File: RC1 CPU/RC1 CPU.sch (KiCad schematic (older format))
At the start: 43 parts, among them J1 Expansion, J2 RC1_UI_Port, J3 BARREL_JACK, M1 Mounting, M2 Mounting, M3 Mounting, M4 Mounting, U1 WD65C02, U2 HM62256BLP-7, U3 28C256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

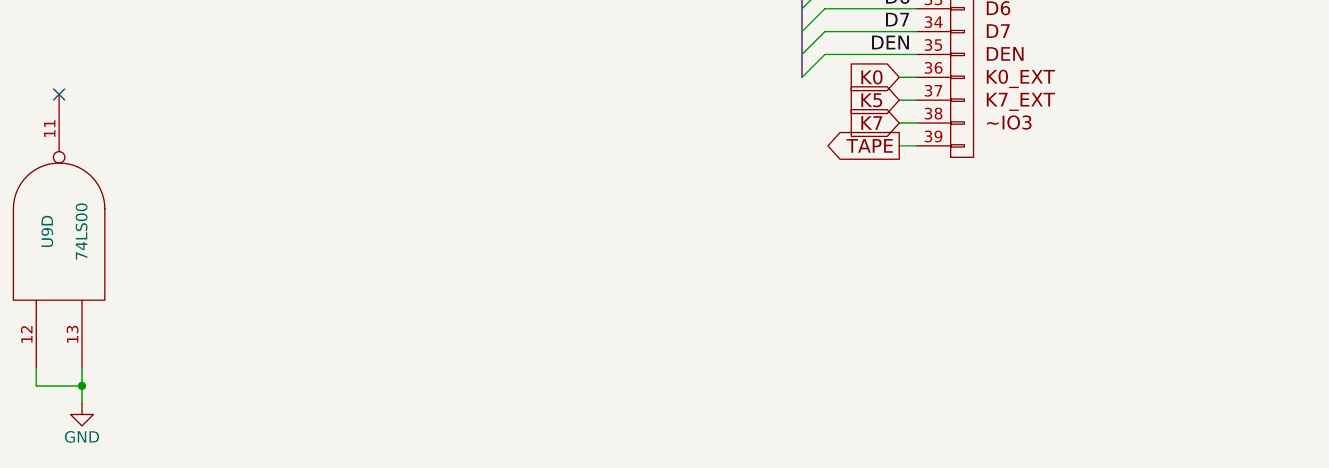
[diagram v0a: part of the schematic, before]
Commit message: Tweaked silkscreens and exported gerbers for CPU/UI
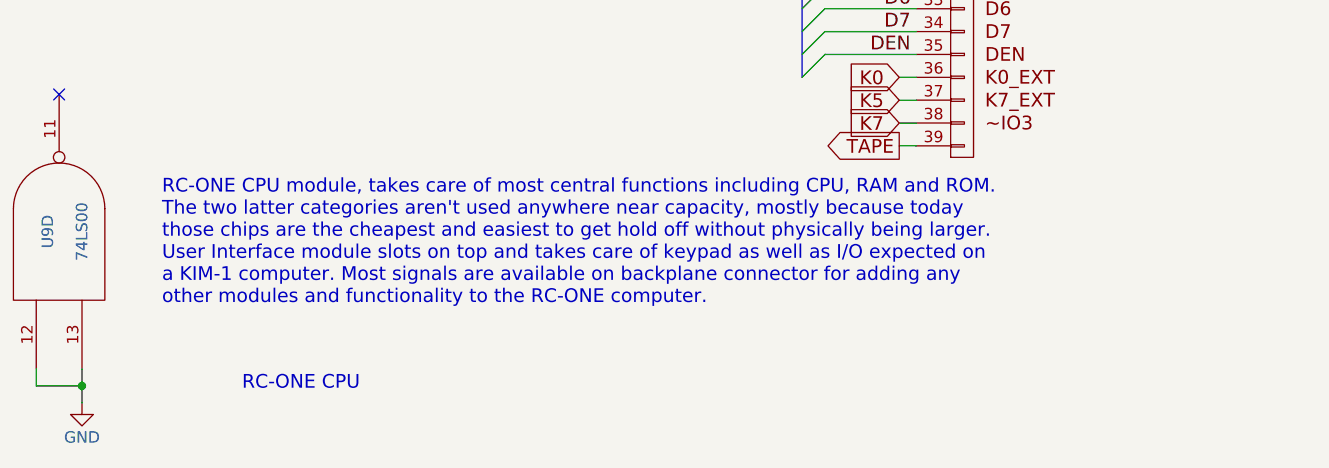
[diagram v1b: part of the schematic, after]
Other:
- note added: "RC-ONE CPU"
- note added: "RC-ONE CPU module, takes care of most central functions including CPU, RAM and ROM.\nThe two latter categories aren't used anywhere near capacity, mostly because today\nthose chips are the cheapest and easiest to get hold off without physically being larger.\nUser Interface module slots on top and takes care of keypad as well as I/O expected on\na KIM-1 computer. Most signals are available on bac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"
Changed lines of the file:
@@
 Wire Wire Line
 	5925 9375 5650 9375
+Text Notes 12175 10925 0    60   ~ 0
+RC-ONE CPU
+Text Notes 11825 10550 0    60   ~ 0
+RC-ONE CPU module, takes care of most central functions including CPU, RAM and ROM.\nThe two latter categories aren't used anywhere near capacity, mostly because today\nthose chips are the cheapest and easiest to get hold off without physically being larger.\nUser Interface module slots on top and takes care of keypad as well as I/O expected on\na KIM-1 computer. Most signals are available on backplane connector for adding any\nother modules and functionality to the RC-ONE computer.
 $EndSCHEMATC

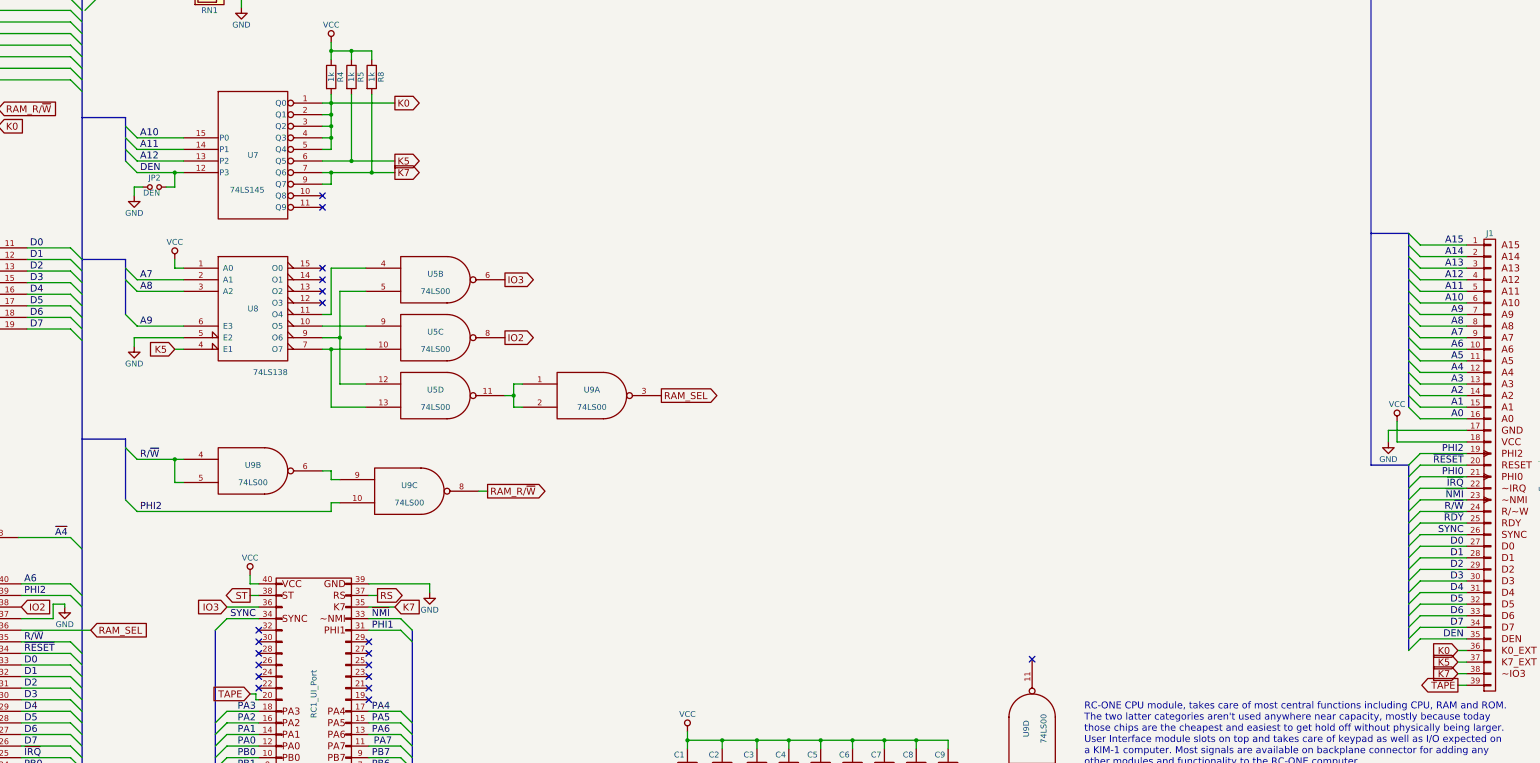
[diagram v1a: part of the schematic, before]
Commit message: Added ability to override K0/K7
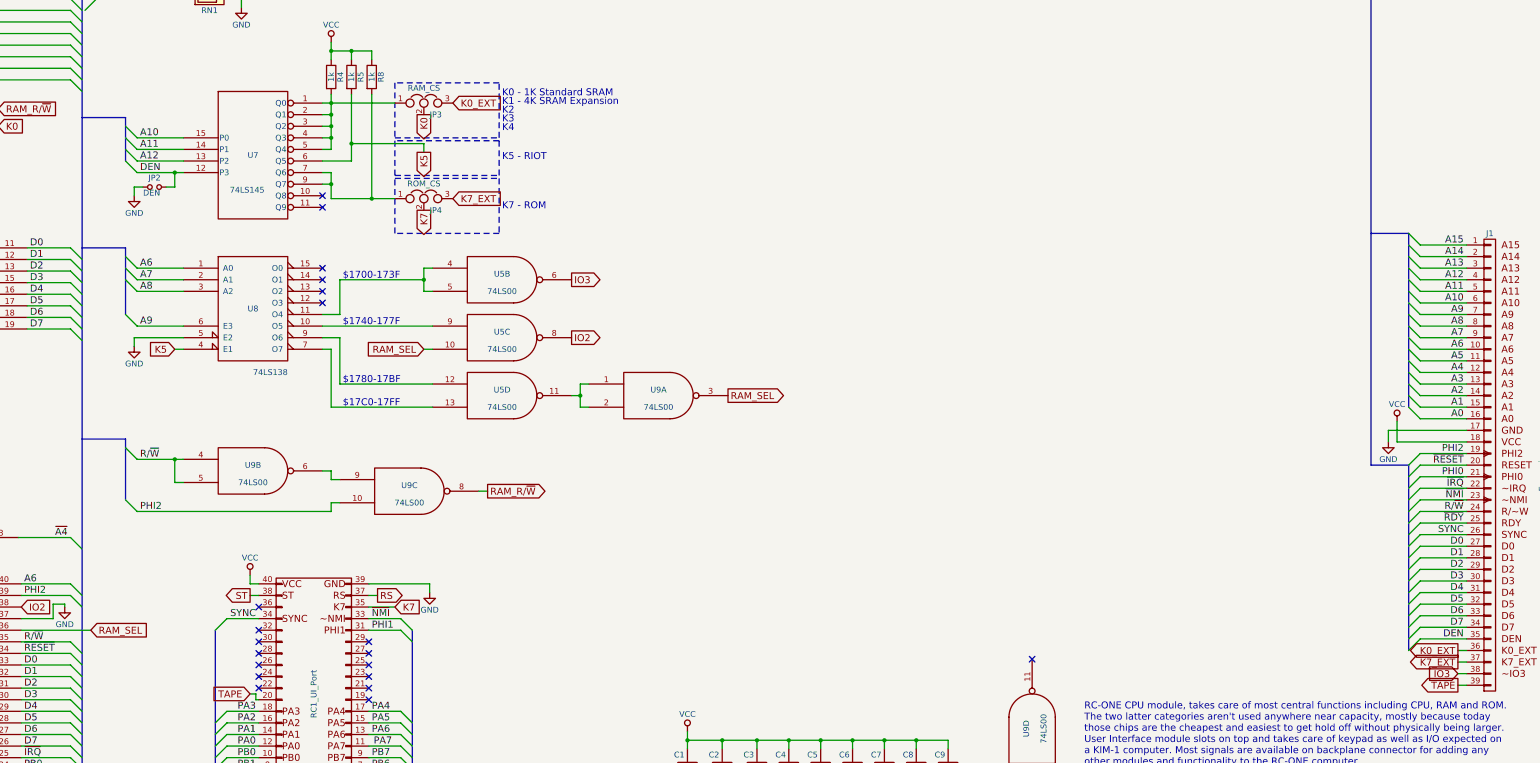
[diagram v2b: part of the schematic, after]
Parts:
- added JP3: RAM_CS, Pin_Headers:Pin_Header_Straight_1x03_Pitch2.54mm, symbol Jumper_NC_Dual
- added JP4: ROM_CS, Pin_Headers:Pin_Header_Straight_1x03_Pitch2.54mm, symbol Jumper_NC_Dual
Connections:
- net A6: now also U8.1 (A0)
- net IO3: now also J1.38 (P38); no longer J2.36 (P36)
- net K0: now also JP3.2; no longer J1.36 (RX), R4.2, U7.1 (Q0), U7.2 (Q1), U7.3 (Q2), U7.4 (Q3), U7.5 (Q4)
- net K5: no longer J1.37 (NMI)
- net K7: now also JP4.2; no longer J1.38 (P38), R8.2, U7.7 (Q6), U7.9 (Q7)
- net RAM_SEL: now also U5.10
- net VCC: no longer U8.1 (A0)
- net at U5.4, U8.11 (O4): now also U5.5
- net at U5.13, U8.7 (O7): no longer U5.10
- net at U5.12, U8.9 (O6): no longer U5.5
- new net: JP3.1, R4.2, U7.1 (Q0), U7.2 (Q1), U7.3 (Q2), U7.4 (Q3), U7.5 (Q4)
- new net: JP4.1, R8.2, U7.7 (Q6), U7.9 (Q7)
- new net K0_EXT: J1.36 (RX), JP3.3
- new net K7_EXT: J1.37 (NMI), JP4.3
- no-connect marks 25 -> 26
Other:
- note added: "$1700-173F"
- note added: "$1740-177F"
- note added: "$1780-17BF"
- note added: "$17C0-17FF"
- note added: "K0 - 1K Standard SRAM"
- note added: "K1 - 4K SRAM Expansion"
- note added: "K2"
- note added: "K3"
- note added: "K4"
- note added: "K5 - RIOT"
- note added: "K7 - ROM"
- moved on the sheet: U5B, U5C, U5D, U9A

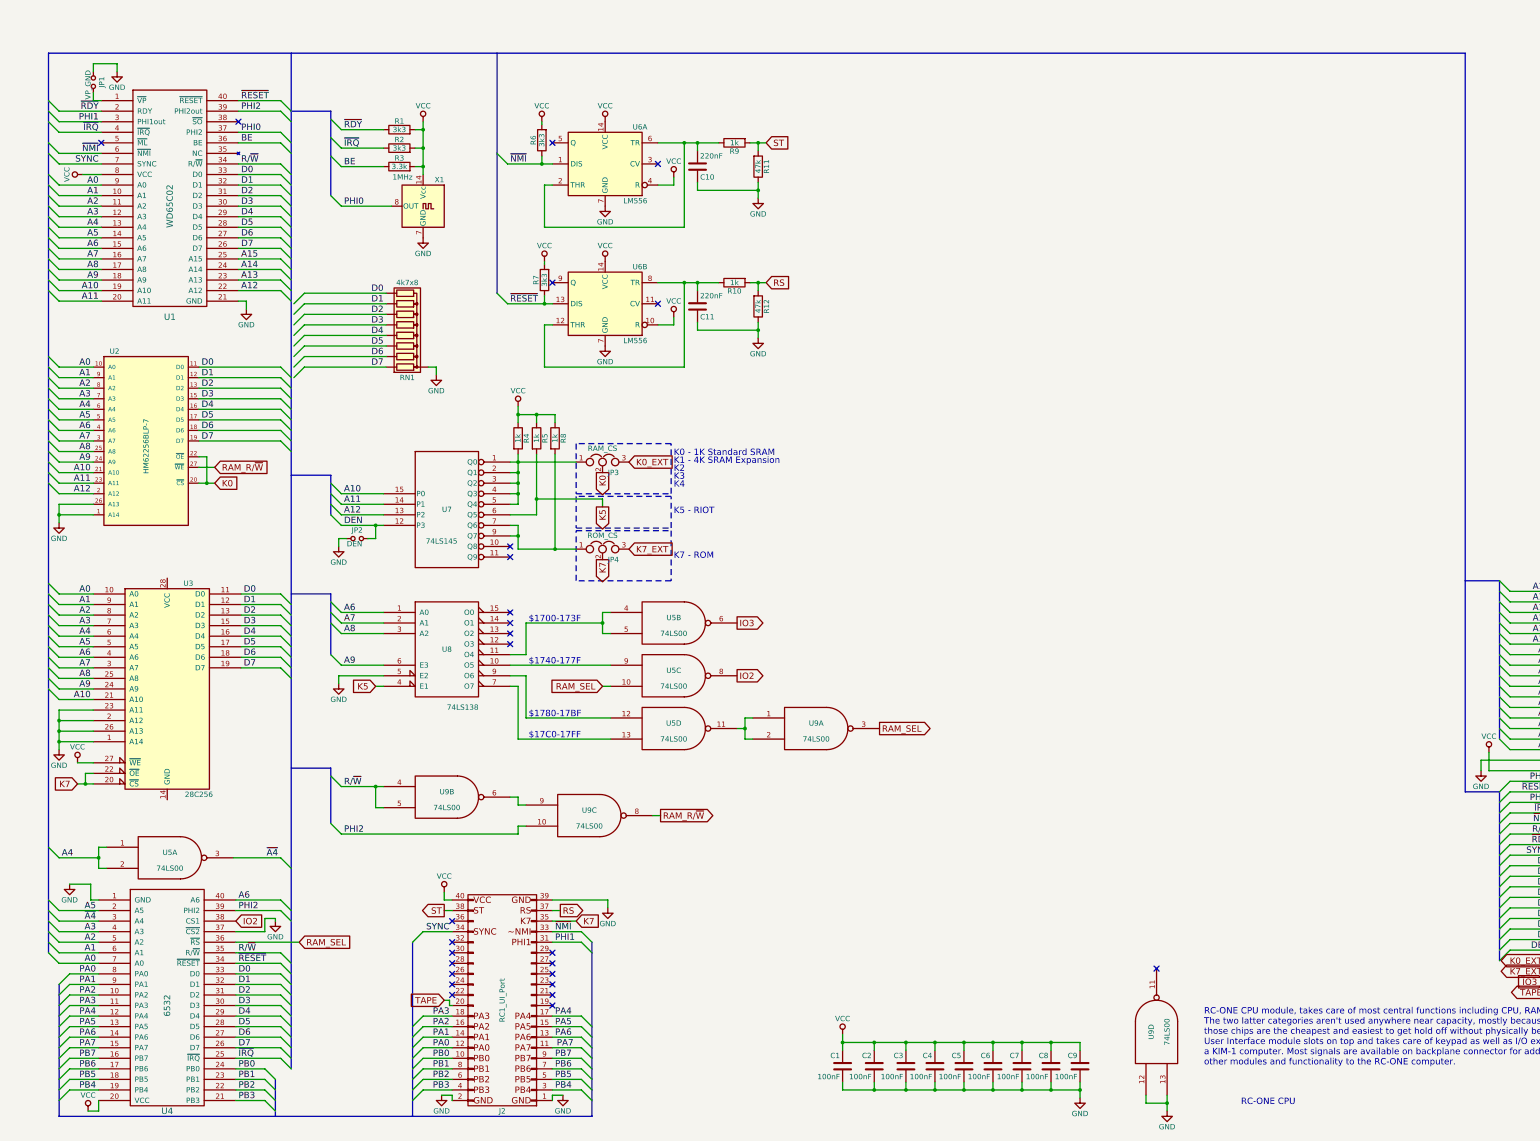
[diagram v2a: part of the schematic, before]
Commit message: Added RAM A13/A14 reconnects for external RAM logic
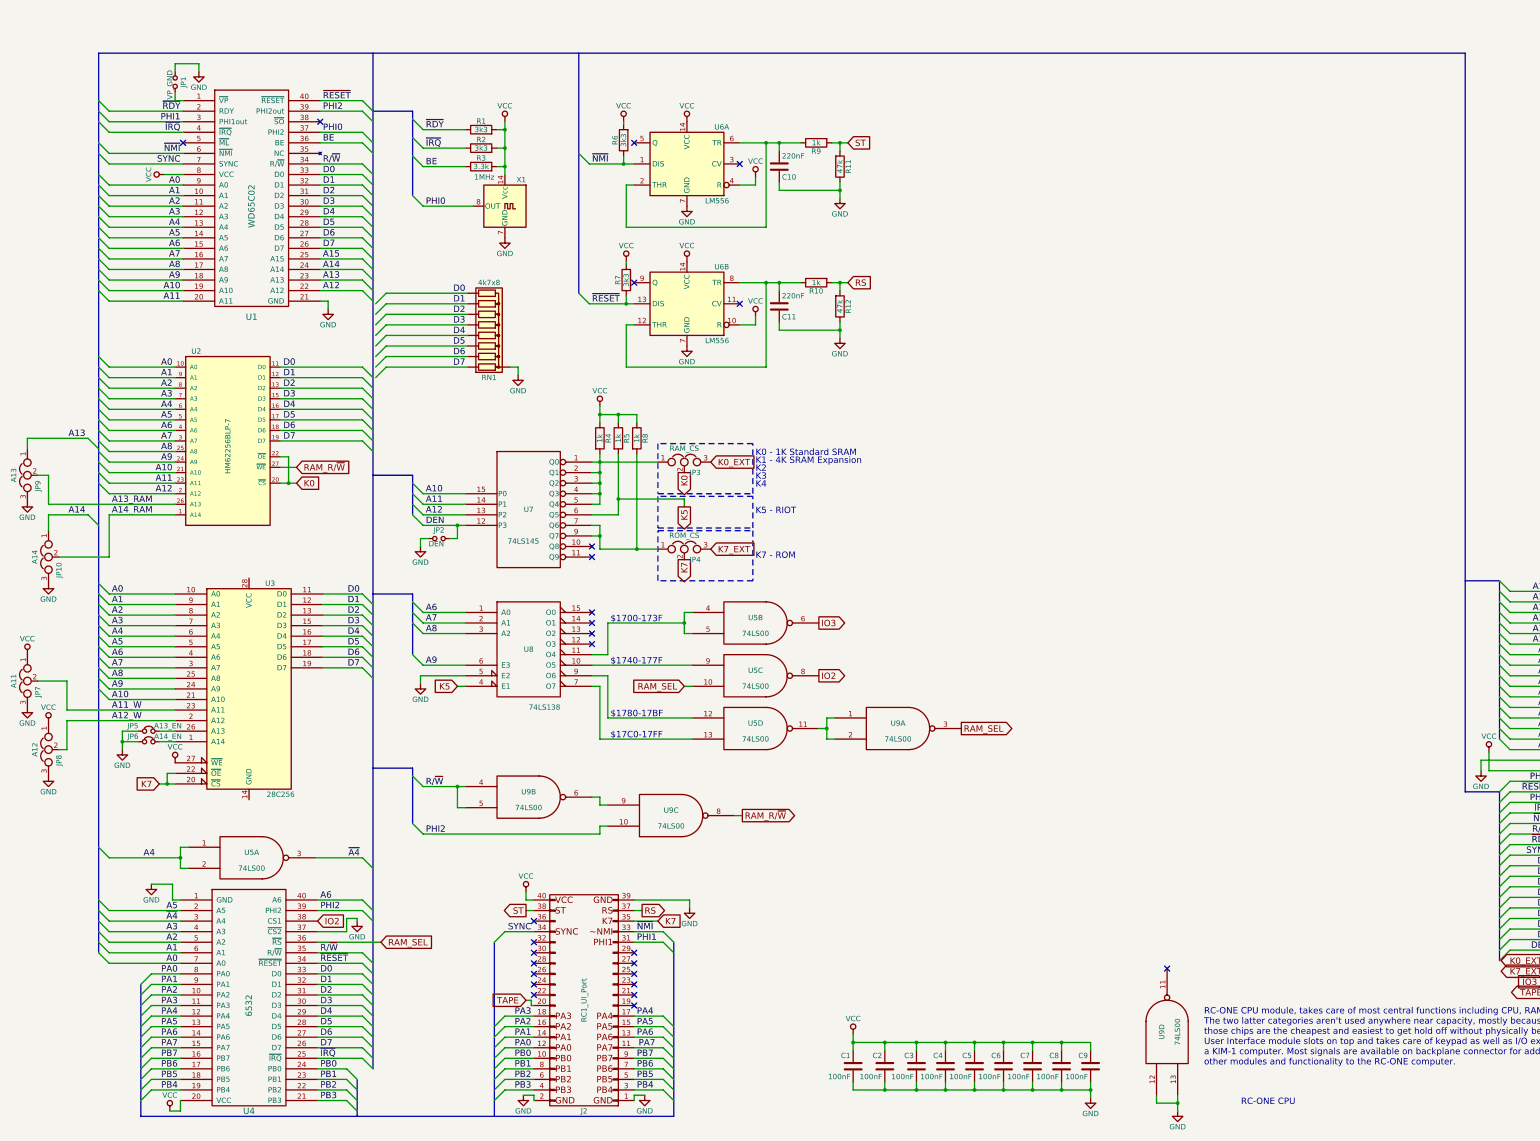
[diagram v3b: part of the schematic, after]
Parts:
- added JP10: A14, Pin_Headers:Pin_Header_Straight_1x03_Pitch2.54mm, symbol Jumper_NC_Dual
- added JP5: A13_EN, Pin_Headers:Pin_Header_Straight_1x02_Pitch2.54mm, symbol Jumper_NC_Small
- added JP6: A14_EN, Pin_Headers:Pin_Header_Straight_1x02_Pitch2.54mm, symbol Jumper_NC_Small
- added JP7: A11, Pin_Headers:Pin_Header_Straight_1x03_Pitch2.54mm, symbol Jumper_NC_Dual
- added JP8: A12, Pin_Headers:Pin_Header_Straight_1x03_Pitch2.54mm, symbol Jumper_NC_Dual
- added JP9: A13, Pin_Headers:Pin_Header_Straight_1x03_Pitch2.54mm, symbol Jumper_NC_Dual
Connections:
- net A13: now also JP9.1
- net A14: now also JP10.1
- net GND: now also JP10.3, JP5.1, JP6.1, JP7.3, JP8.3, JP9.3; no longer U2.1 (A14), U2.26 (A13), U3.1 (A14), U3.2 (A12), U3.23 (A11), U3.26 (A13)
- net VCC: now also JP7.1, JP8.1
- new net: JP6.2, U3.1 (A14)
- new net: JP5.2, U3.26 (A13)
- new net A11_W: JP7.2, U3.23 (A11)
- new net A12_W: JP8.2, U3.2 (A12)
- new net A13_RAM: JP9.2, U2.26 (A13)
- new net A14_RAM: JP10.2, U2.1 (A14)
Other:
- moved on the sheet: C1, C10, C11, C2, C3, C4, C5, C6, C7, C8, C9, J2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
